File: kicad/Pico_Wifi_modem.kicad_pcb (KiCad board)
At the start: 2 copper layers, 100 x 66.1 mm, 39 parts, among them CON1 BARREL_JACK, P1 CONN_02X05, U1 MAX3237CAI+, U2 74HCT245, U3 Pico, U4 LM2950ACZ-3.3, U5 24LC32

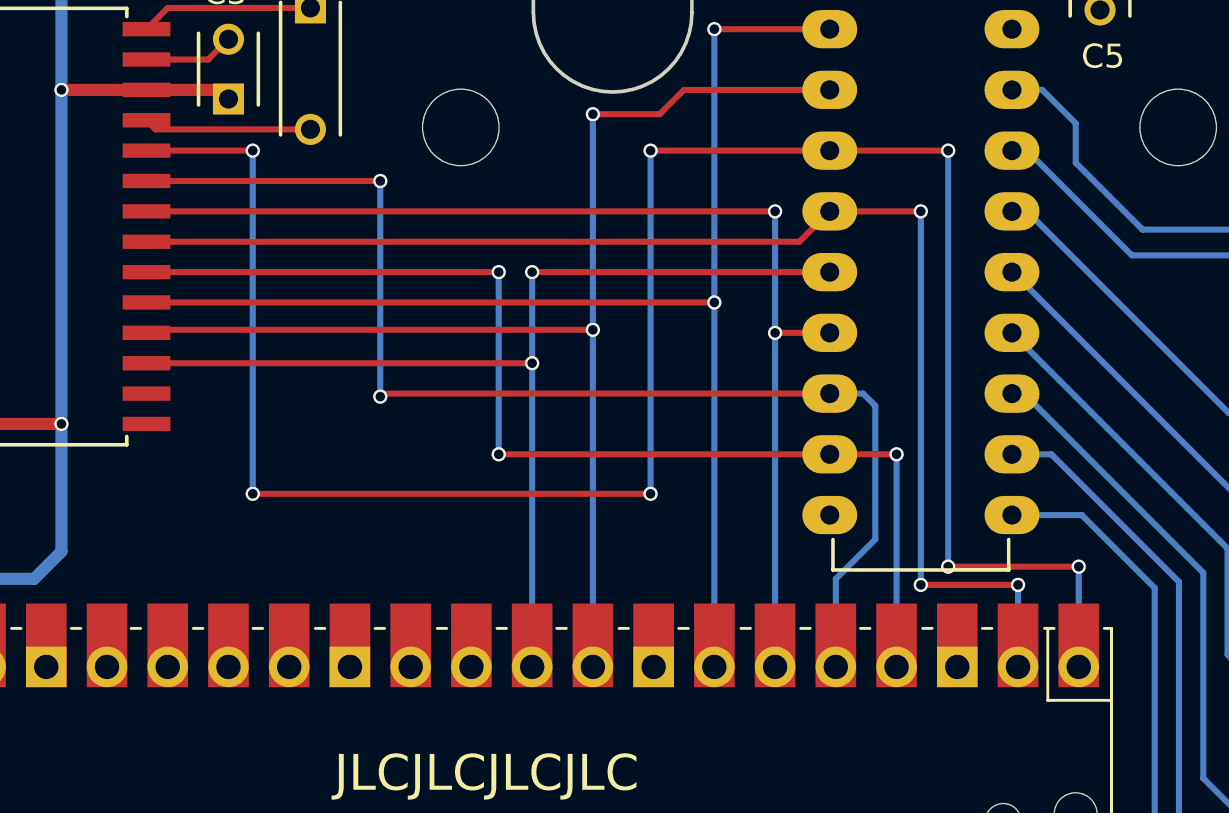
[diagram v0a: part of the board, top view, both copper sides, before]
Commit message: Had the SD & RD LEDs reversed: fixed It'd be easy enough to criss cross R3 and R4 and use the original PCB, but it was easy enough to fix as well.
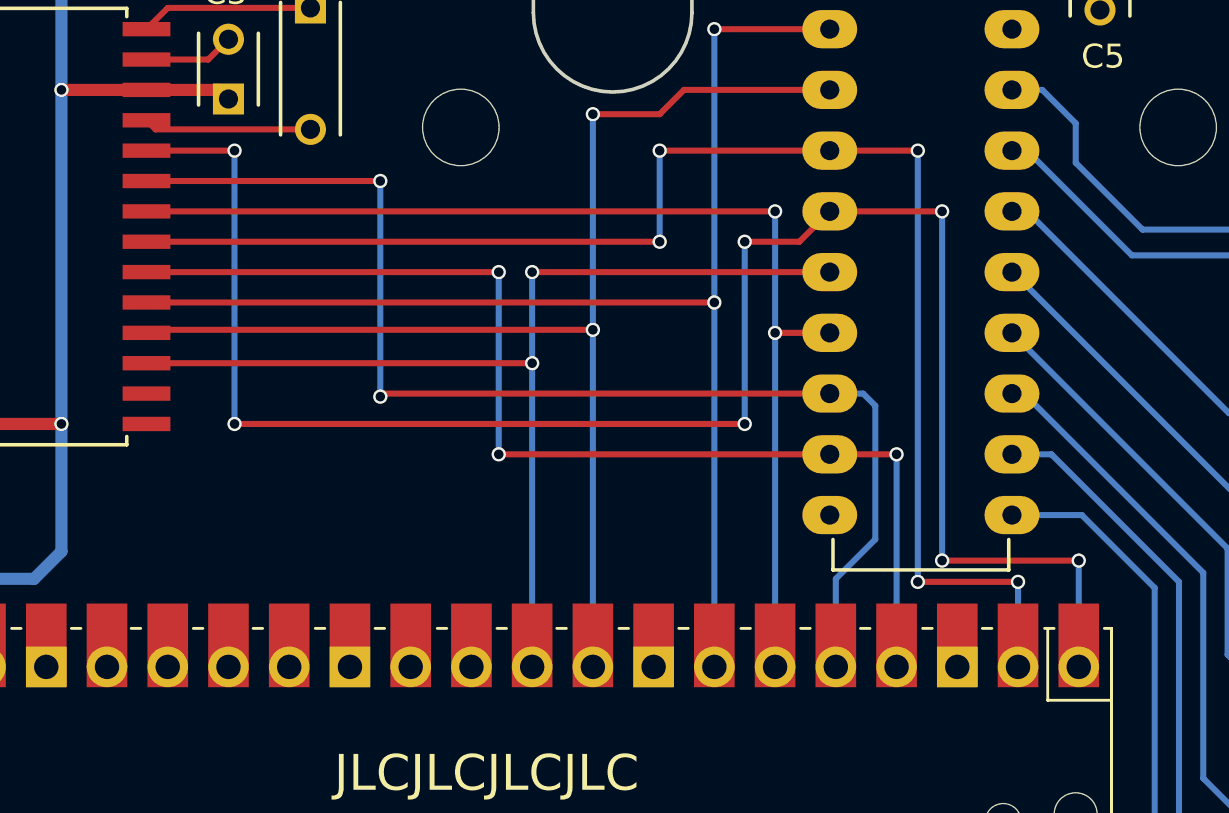
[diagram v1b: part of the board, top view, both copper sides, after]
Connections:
- U2 pad 4: Net-(U1-Pad24) -> Net-(U1-Pad21)
- U2 pad 5: Net-(U1-Pad21) -> Net-(U1-Pad24)
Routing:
- net Net-(U1-Pad24): track 89.3 -> 77.6 mm
- net Net-(U1-Pad21): track 56.0 -> 61.8 mm, vias 3 -> 5
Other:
- board text added: "Pico Wifi modem Vers 0.2 Oct 15 2022"
- board text removed: "Pico Wifi modem Vers 0.1 Oct 5 2022"
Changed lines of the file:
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@@
     (links 136)
     (no_connects 0)
-    (area 105.634379 74.884 210.138 142.045001)
+    (area 109.644999 75.754999 209.795001 142.045001)
     (thickness 1.6)
     (drawings 30)
-    (tracks 239)
+    (tracks 243)
     (zones 0)
     (modules 39)
@@
       (net 41 "Net-(U1-Pad18)"))
     (pad 4 thru_hole oval (at 0 7.62 180) (size 2.3 1.6) (drill 0.8) (layers *.Cu *.Mask)
+      (net 44 "Net-(U1-Pad21)"))
+    (pad 5 thru_hole oval (at 0 10.16 180) (size 2.3 1.6) (drill 0.8) (layers *.Cu *.Mask)
       (net 47 "Net-(U1-Pad24)"))
-    (pad 5 thru_hole oval (at 0 10.16 180) (size 2.3 1.6) (drill 0.8) (layers *.Cu *.Mask)
-      (net 44 "Net-(U1-Pad21)"))
     (pad 6 thru_hole oval (at 0 12.7 180) (size 2.3 1.6) (drill 0.8) (layers *.Cu *.Mask)
       (net 40 "Net-(U1-Pad17)"))
@@
     (effects (font (size 1.5 1.5) (thickness 0.3)))
   )
-  (gr_text "Pico Wifi modem\nVers 0.1\nOct 5 2022" (at 163.957 114.173) (layer B.SilkS)
+  (gr_text "Pico Wifi modem\nVers 0.2\nOct 15 2022" (at 163.957 114.173) (layer B.SilkS)
     (effects (font (size 1.5 1.5) (thickness 0.3)) (justify mirror))
   )
@@
   (segment (start 161.036 99.441) (end 161.036 91.821) (width 0.254) (layer B.Cu) (net 43))
   (via (at 161.036 99.441) (size 0.6) (drill 0.4) (layers F.Cu B.Cu) (net 43))
-  (segment (start 182.753 108.331) (end 182.753 104.902) (width 0.254) (layer B.Cu) (net 44))
-  (segment (start 178.689 89.281) (end 174.879 89.281) (width 0.254) (layer F.Cu) (net 44))
-  (via (at 178.689 89.281) (size 0.6) (drill 0.4) (layers F.Cu B.Cu) (net 44))
-  (segment (start 178.689 104.902) (end 178.689 89.281) (width 0.254) (layer B.Cu) (net 44))
-  (via (at 178.689 104.902) (size 0.6) (drill 0.4) (layers F.Cu B.Cu) (net 44))
-  (segment (start 182.753 104.902) (end 178.689 104.902) (width 0.254) (layer F.Cu) (net 44))
-  (via (at 182.753 104.902) (size 0.6) (drill 0.4) (layers F.Cu B.Cu) (net 44))
-  (segment (start 146.305 90.551) (end 173.609 90.551) (width 0.254) (layer F.Cu) (net 44))
-  (segment (start 173.609 90.551) (end 174.879 89.281) (width 0.254) (layer F.Cu) (net 44))
+  (segment (start 174.879 86.741) (end 167.767 86.741) (width 0.254) (layer F.Cu) (net 44))
+  (segment (start 167.767 90.551) (end 146.305 90.551) (width 0.254) (layer F.Cu) (net 44))
+  (via (at 167.767 90.551) (size 0.6) (drill 0.4) (layers F.Cu B.Cu) (net 44))
+  (segment (start 167.767 86.741) (end 167.767 90.551) (width 0.254) (layer B.Cu) (net 44))
+  (via (at 167.767 86.741) (size 0.6) (drill 0.4) (layers F.Cu B.Cu) (net 44))
+  (segment (start 182.753 108.331) (end 182.753 104.775) (width 0.254) (layer B.Cu) (net 44))
+  (segment (start 178.562 86.741) (end 174.879 86.741) (width 0.254) (layer F.Cu) (net 44))
+  (via (at 178.562 86.741) (size 0.6) (drill 0.4) (layers F.Cu B.Cu) (net 44))
+  (segment (start 178.562 104.775) (end 178.562 86.741) (width 0.254) (layer B.Cu) (net 44))
+  (via (at 178.562 104.775) (size 0.6) (drill 0.4) (layers F.Cu B.Cu) (net 44))
+  (segment (start 182.753 104.775) (end 178.562 104.775) (width 0.254) (layer F.Cu) (net 44))
+  (via (at 182.753 104.775) (size 0.6) (drill 0.4) (layers F.Cu B.Cu) (net 44))
   (segment (start 172.593 94.361) (end 172.593 108.331) (width 0.254) (layer B.Cu) (net 45))
   (segment (start 146.305 89.281) (end 172.593 89.281) (width 0.254) (layer F.Cu) (net 45))
@@
   (segment (start 156.083 88.011) (end 156.083 97.028) (width 0.254) (layer B.Cu) (net 46))
   (via (at 156.083 88.011) (size 0.6) (drill 0.4) (layers F.Cu B.Cu) (net 46))
-  (segment (start 185.293 108.331) (end 185.293 104.14) (width 0.254) (layer B.Cu) (net 47))
-  (segment (start 179.832 86.741) (end 174.879 86.741) (width 0.254) (layer F.Cu) (net 47))
-  (via (at 179.832 86.741) (size 0.6) (drill 0.4) (layers F.Cu B.Cu) (net 47))
-  (segment (start 179.832 104.14) (end 179.832 86.741) (width 0.254) (layer B.Cu) (net 47))
-  (via (at 179.832 104.14) (size 0.6) (drill 0.4) (layers F.Cu B.Cu) (net 47))
-  (segment (start 185.293 104.14) (end 179.832 104.14) (width 0.254) (layer F.Cu) (net 47))
-  (via (at 185.293 104.14) (size 0.6) (drill 0.4) (layers F.Cu B.Cu) (net 47))
-  (segment (start 174.879 86.741) (end 167.386 86.741) (width 0.254) (layer F.Cu) (net 47))
-  (segment (start 150.749 86.741) (end 146.305 86.741) (width 0.254) (layer F.Cu) (net 47))
-  (via (at 150.749 86.741) (size 0.6) (drill 0.4) (layers F.Cu B.Cu) (net 47))
-  (segment (start 150.749 101.092) (end 150.749 86.741) (width 0.254) (layer B.Cu) (net 47))
-  (via (at 150.749 101.092) (size 0.6) (drill 0.4) (layers F.Cu B.Cu) (net 47))
-  (segment (start 167.386 101.092) (end 150.749 101.092) (width 0.254) (layer F.Cu) (net 47))
-  (via (at 167.386 101.092) (size 0.6) (drill 0.4) (layers F.Cu B.Cu) (net 47))
-  (segment (start 167.386 86.741) (end 167.386 101.092) (width 0.254) (layer B.Cu) (net 47))
-  (via (at 167.386 86.741) (size 0.6) (drill 0.4) (layers F.Cu B.Cu) (net 47))
+  (segment (start 174.879 89.281) (end 173.609 90.551) (width 0.254) (layer F.Cu) (net 47))
+  (segment (start 149.987 86.741) (end 146.305 86.741) (width 0.254) (layer F.Cu) (net 47))
+  (via (at 149.987 86.741) (size 0.6) (drill 0.4) (layers F.Cu B.Cu) (net 47))
+  (segment (start 149.987 98.171) (end 149.987 86.741) (width 0.254) (layer B.Cu) (net 47))
+  (via (at 149.987 98.171) (size 0.6) (drill 0.4) (layers F.Cu B.Cu) (net 47))
+  (segment (start 171.323 98.171) (end 149.987 98.171) (width 0.254) (layer F.Cu) (net 47))
+  (via (at 171.323 98.171) (size 0.6) (drill 0.4) (layers F.Cu B.Cu) (net 47))
+  (segment (start 171.323 90.551) (end 171.323 98.171) (width 0.254) (layer B.Cu) (net 47))
+  (via (at 171.323 90.551) (size 0.6) (drill 0.4) (layers F.Cu B.Cu) (net 47))
+  (segment (start 173.609 90.551) (end 171.323 90.551) (width 0.254) (layer F.Cu) (net 47))
+  (segment (start 185.293 108.331) (end 185.293 103.886) (width 0.254) (layer B.Cu) (net 47))
+  (segment (start 179.578 89.281) (end 174.879 89.281) (width 0.254) (layer F.Cu) (net 47))
+  (via (at 179.578 89.281) (size 0.6) (drill 0.4) (layers F.Cu B.Cu) (net 47))
+  (segment (start 179.578 103.886) (end 179.578 89.281) (width 0.254) (layer B.Cu) (net 47))
+  (via (at 179.578 103.886) (size 0.6) (drill 0.4) (layers F.Cu B.Cu) (net 47))
+  (segment (start 185.293 103.886) (end 179.578 103.886) (width 0.254) (layer F.Cu) (net 47))
+  (via (at 185.293 103.886) (size 0.6) (drill 0.4) (layers F.Cu B.Cu) (net 47))
   (zone (net 0) (net_name "") (layer F.Cu) (hatch edge 0.508)
     (connect_pads (clearance 0.508))
